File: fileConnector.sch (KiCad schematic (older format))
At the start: 7 parts, among them J2 TE_Eurocard_96pole

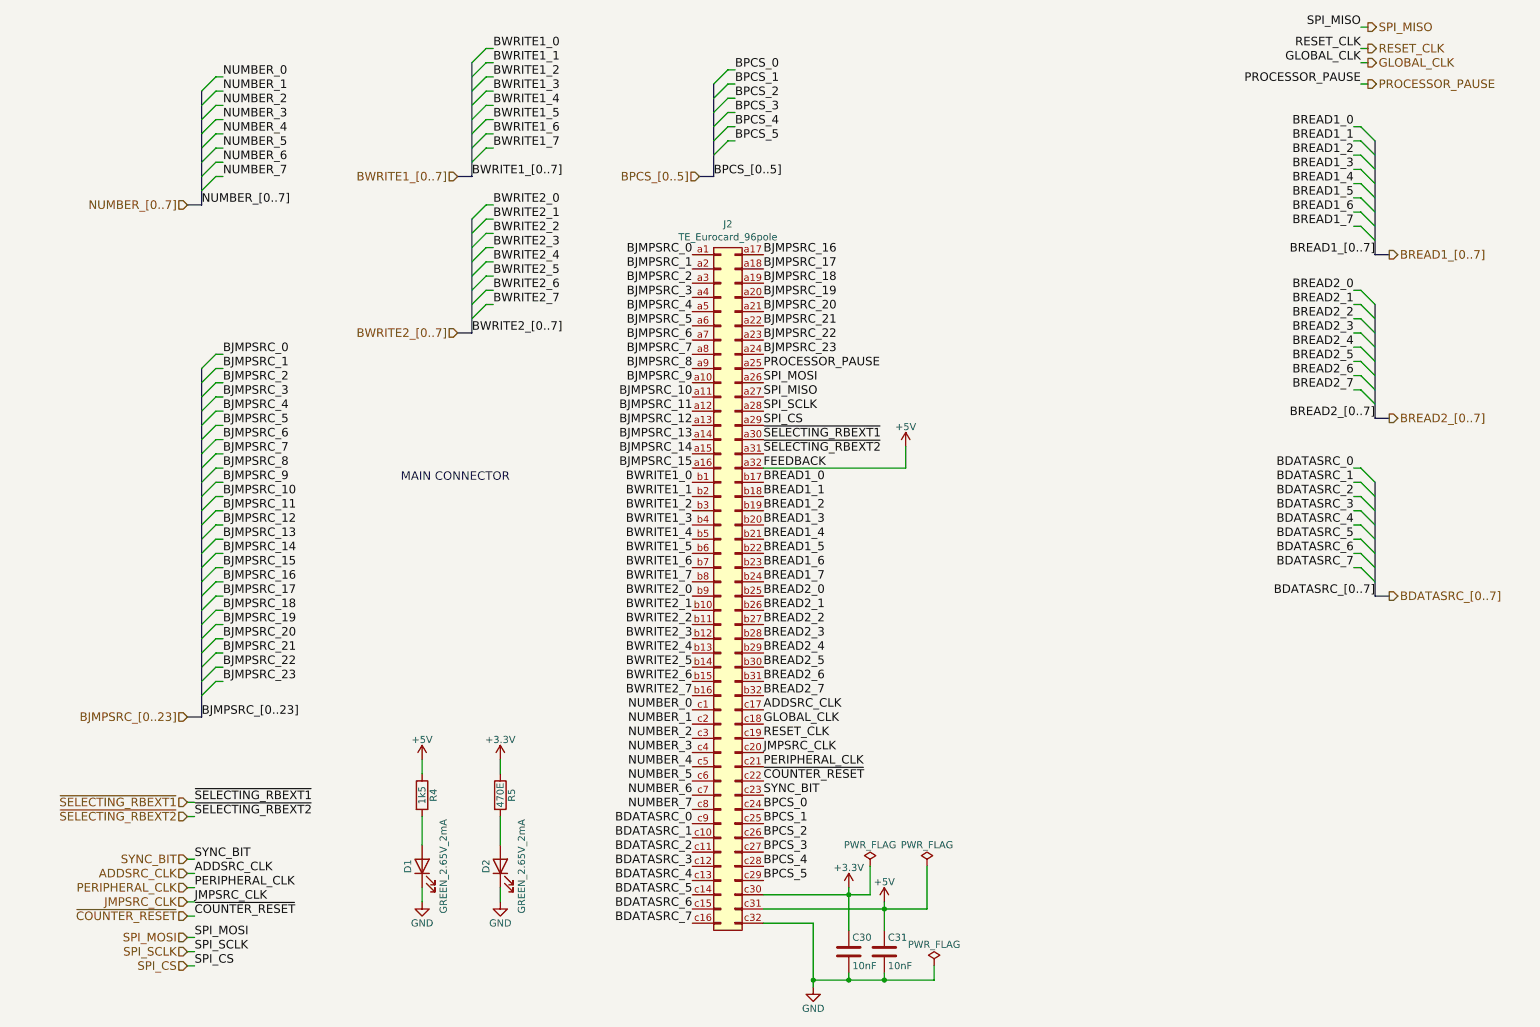
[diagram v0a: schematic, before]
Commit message: Better decoupling #6
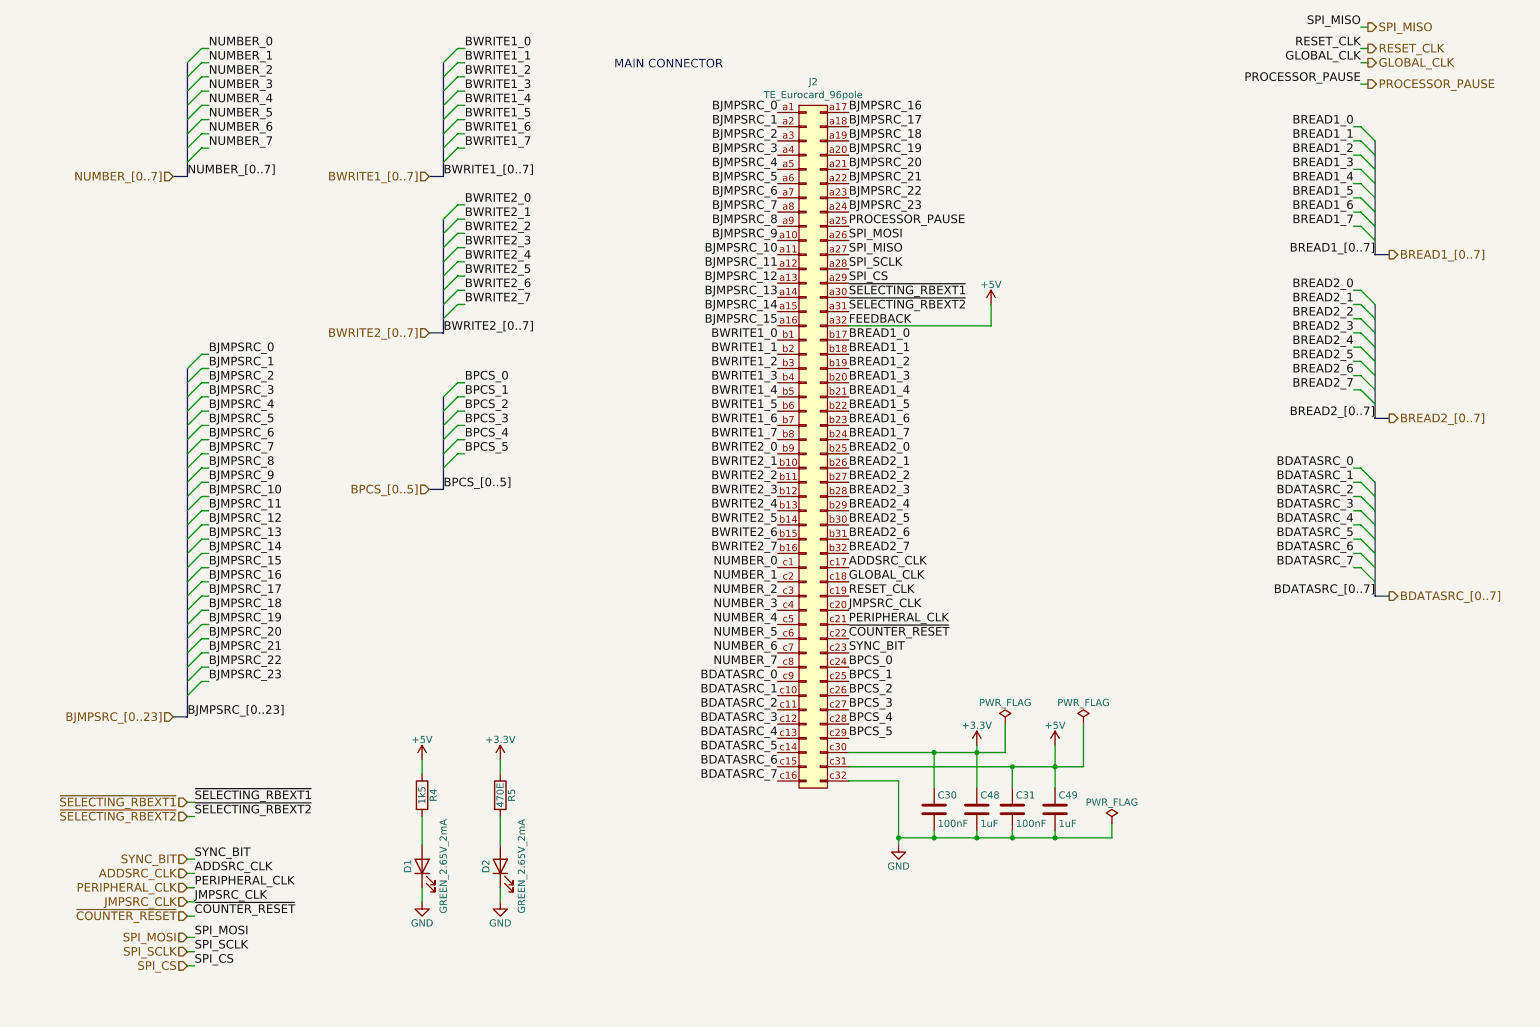
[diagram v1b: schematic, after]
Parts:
- added C48, C49: 1uF, Capacitor_SMD:C_0805_2012Metric, symbol Device:C
- C30, C31: value 10nF -> 100nF
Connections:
- net +3V3: now also C48.1
- net +5V: now also C49.1
- net GND: now also C48.2, C49.2
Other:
- moved on the sheet: C30, C31, J2
